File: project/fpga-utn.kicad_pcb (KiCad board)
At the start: 2 copper layers, 76 parts, among them J1 USB_C_Receptacle_USB2.0_16P, U1 LD1117S33TR_SOT223, U2 LD1117S12TR_SOT223, U3 USBLC6-2SC6, U4 FT2232HL, U5 M93C66, U6 ICE40HX4K-TQ144, U7 W25X40CLSN, X1 ECS-3225MV-120-BN-TR

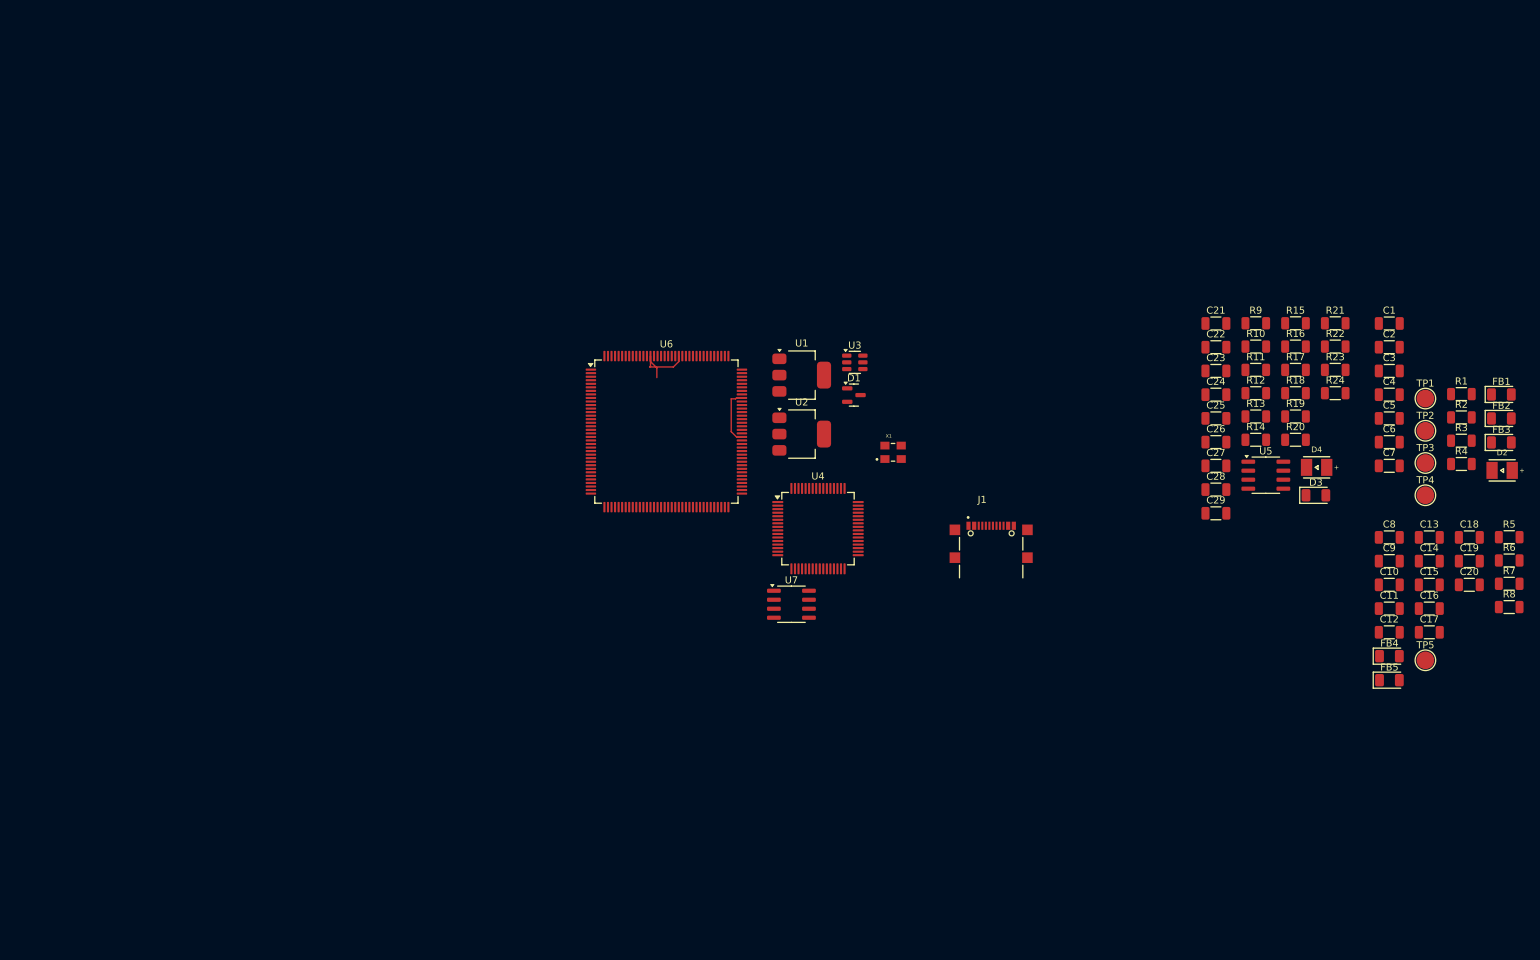
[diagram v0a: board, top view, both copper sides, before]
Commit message: Eliminación de archivos de respaldo y correcciones en la biblioteca de componentes. Se eliminaron archivos de autosave, archivos de esquemas y modelos 3D no utilizados, así como modificaciones en las propiedades de algunos componentes en la biblioteca.
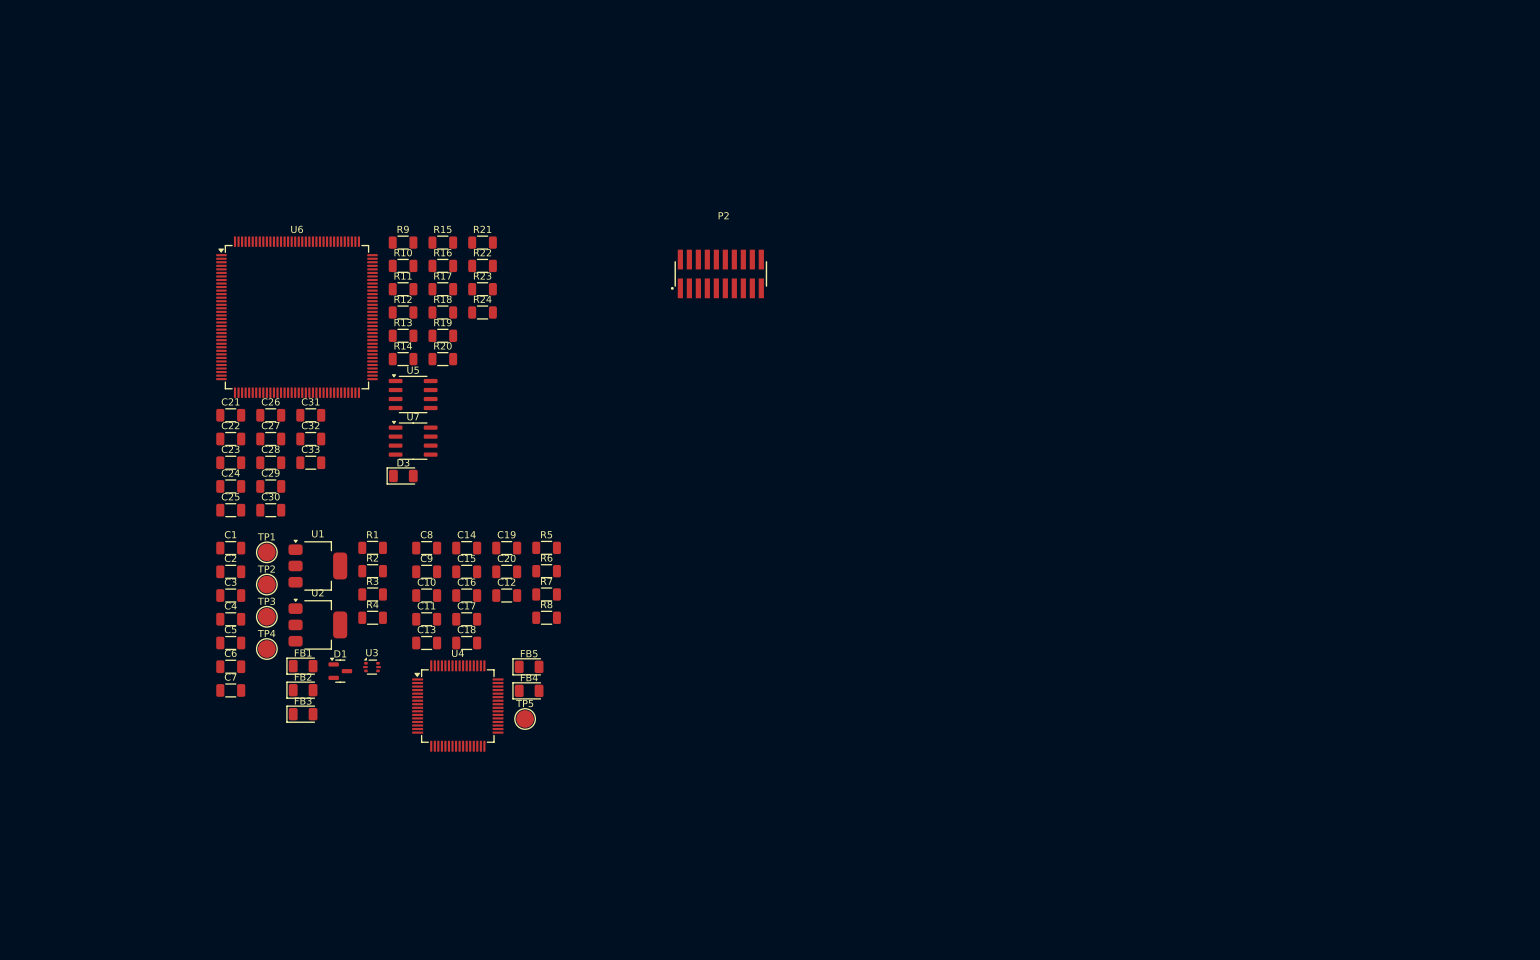
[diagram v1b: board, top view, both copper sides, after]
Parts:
- removed D2, D4: LED, libraries:WL-SMTW_3528
- removed J1: USB_C_Receptacle_USB2.0_16P, libraries:AMPHENOL_GSB1C41110SSHR
- removed X1: ECS-3225MV-120-BN-TR, libraries:OSC_ECS-3225MV-120-BN-TR
- added C30: 100n, Capacitor_SMD:C_1206_3216Metric, F.Cu at (83.5, 87.7)
- added C31: 100n, Capacitor_SMD:C_1206_3216Metric, F.Cu at (89.1, 74.3)
- added C32: 100n, Capacitor_SMD:C_1206_3216Metric, F.Cu at (89.1, 77.7)
- added C33: 100n, Capacitor_SMD:C_1206_3216Metric, F.Cu at (89.1, 81.0)
- added P2: Conector SMD 2x10, FRT-FPGA:Header 2x10 SMD, F.Cu at (147.2, 54.1)
- C21: value 100n -> 10u
- C22: value 10n -> 100n
- C23, C25: value 1u -> 100n
- C24: value 10n -> 10u
- C26, C28: value 10u -> 10n
- C27, C29: value 100n -> 1u
- R10: value 10k -> 2k2
- R11: value 10k -> 100
- R12, R20: value 220 -> 10k
- R13: value R -> 10k
- R14: value R -> 220
- R17, R18: value 10k -> R
- R19: value 220R -> 10k
- R21: value 220 -> 220R
- R22: value 1k -> 220
- R23: value 100 -> 220
- R24: value 100 -> 1k
- R9: value 2k2 -> 100
- U3: footprint Package_TO_SOT_SMD:SOT-23-6 -> Package_TO_SOT_SMD:SOT-666
- moved FB1 173.5 mm to (88.1, 109.7)
- moved FB2 173.5 mm to (88.1, 113.1)
- moved FB3 173.5 mm to (88.1, 116.5)
- moved C1 166.6 mm to (77.8, 93.1)
- moved C2 166.6 mm to (77.8, 96.4)
- moved C3 166.6 mm to (77.8, 99.8)
- moved C4 166.6 mm to (77.8, 103.1)
- moved C5 166.6 mm to (77.8, 106.5)
- moved C6 166.6 mm to (77.8, 109.8)
- moved C7 166.6 mm to (77.8, 113.2)
- moved TP1 165.0 mm to (82.9, 93.7)
- moved TP2 165.0 mm to (82.9, 98.2)
- moved TP3 165.0 mm to (82.9, 102.8)
- moved TP4 165.0 mm to (82.9, 107.3)
- moved R1 155.2 mm to (97.9, 93.0)
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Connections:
- net /FPGA/VUART_CTS renamed /Perifericos/VUART_CTS
- net /FPGA/VUART_DCD renamed /Perifericos/VUART_DCD
- net /FPGA/VUART_DSR renamed /Perifericos/VUART_DSR
- net /FPGA/VUART_DTR renamed /Perifericos/VUART_DTR
- net /FPGA/VUART_RTS renamed /Perifericos/VUART_RTS
- net /FPGA/VUART_Rx renamed /Perifericos/VUART_Rx
- net /FPGA/VUART_Tx renamed /Perifericos/VUART_Tx
- net /Memorias/EEPROM_CLK renamed /Memorias y PLL/EEPROM_CLK
- net /Memorias/EEPROM_CS renamed /Memorias y PLL/EEPROM_CS
- net /Memorias/Flash_SCK renamed /Memorias y PLL/Flash_SCK
- C21 pad 1: +3V3 -> /Memorias y PLL/GNDPLL1
- C21 pad 2: GND -> /Memorias y PLL/VCCPLL1
- C22 pad 1: +3V3 -> /Memorias y PLL/GNDPLL1
- C22 pad 2: GND -> /Memorias y PLL/VCCPLL1
- C24 pad 1: +3V3 -> /Memorias y PLL/VCCPLL2
- C24 pad 2: GND -> /Memorias y PLL/GNDPLL2
- C25 pad 1: +3V3 -> /Memorias y PLL/VCCPLL2
- C25 pad 2: GND -> /Memorias y PLL/GNDPLL2
- C26 pad 1: /Memorias/GNDPLL1 -> +3V3
- C26 pad 2: /Memorias/VCCPLL1 -> GND
- C27 pad 1: /Memorias/GNDPLL1 -> +3V3
- C27 pad 2: /Memorias/VCCPLL1 -> GND
- C28 pad 1: /Memorias/VCCPLL2 -> +3V3
- C28 pad 2: /Memorias/GNDPLL2 -> GND
- C29 pad 1: /Memorias/VCCPLL2 -> +3V3
- C29 pad 2: /Memorias/GNDPLL2 -> GND
- R10 pad 1: +3V3 -> /Memorias y PLL/EEPROM_DATA
- R11 pad 1: +3V3 -> +1V2
- R11 pad 2: Net-(U6E-~{CRESET}) -> /Memorias y PLL/VCCPLL2
- R12 pad 1: Net-(U6E-~{CRESET}) -> +3V3
- R12 pad 2: /Memorias/Flash_RESET -> Net-(U5-DO)
- R13 pad 1: /Memorias/Flash_DI -> +3V3
- R13 pad 2: Net-(U6E-IOB_105_SDO) -> Net-(U6E-~{CRESET})
- R14 pad 1: /Memorias/Flash_DO -> Net-(U6E-~{CRESET})
- R14 pad 2: Net-(U6E-IOB_106_SDI) -> /Memorias y PLL/Flash_RESET
- R15 pad 1: unconnected-(R15-Pad1) -> /Memorias y PLL/Flash_DI
- R15 pad 2: Net-(U6E-IOB_107_SCK) -> Net-(U6E-IOB_105_SDO)
- R16 pad 1: /Memorias/Flash_CS -> /Memorias y PLL/Flash_DO
- R16 pad 2: Net-(U6E-IOB_108_SS) -> Net-(U6E-IOB_106_SDI)
- R17 pad 1: +3V3 -> unconnected-(R17-Pad1)
- R17 pad 2: Net-(U6E-IOB_108_SS) -> Net-(U6E-IOB_107_SCK)
- R18 pad 1: +3V3 -> /Memorias y PLL/Flash_CS
- R18 pad 2: Net-(U6E-IOB_107_SCK) -> Net-(U6E-IOB_108_SS)
- R19 pad 1: /Memorias/Flash_DONE -> +3V3
- R19 pad 2: Net-(D4-A) -> Net-(U6E-IOB_108_SS)
- R20 pad 1: Net-(U7-~{WP}) -> +3V3
- R20 pad 2: +3V3 -> Net-(U6E-IOB_107_SCK)
- R21 pad 1: +3V3 -> /Memorias y PLL/Flash_DONE
- R21 pad 2: Net-(U7-~{HOLD}) -> Net-(D4-A)
- R22 pad 1: Net-(D4-A) -> Net-(U7-~{WP})
- R23 pad 1: +1V2 -> +3V3
- R23 pad 2: /Memorias/VCCPLL1 -> Net-(U7-~{HOLD})
- R24 pad 1: +1V2 -> Net-(D4-A)
- R24 pad 2: /Memorias/VCCPLL2 -> +3V3
- R9 pad 1: /Memorias/EEPROM_DATA -> +1V2
- R9 pad 2: Net-(U5-DO) -> /Memorias y PLL/VCCPLL1
- U4 pad 17: /Memorias/Flash_DI -> /Memorias y PLL/Flash_DI
- U4 pad 18: /Memorias/Flash_DO -> /Memorias y PLL/Flash_DO
- U4 pad 21: /Memorias/Flash_CS -> /Memorias y PLL/Flash_CS
- U4 pad 23: /Memorias/Flash_DONE -> /Memorias y PLL/Flash_DONE
- U4 pad 24: /Memorias/Flash_RESET -> /Memorias y PLL/Flash_RESET
- U4 pad 61: /Memorias/EEPROM_DATA -> /Memorias y PLL/EEPROM_DATA
- U5 pad 3: /Memorias/EEPROM_DATA -> /Memorias y PLL/EEPROM_DATA
- U6 pad 111: Net-(U6E-VCC-Pad111) -> +1V2
- U6 pad 126: /Memorias/VCCPLL1 -> /Memorias y PLL/VCCPLL1
- U6 pad 127: /Memorias/GNDPLL1 -> /Memorias y PLL/GNDPLL1
- U6 pad 27: Net-(U6E-VCC-Pad111) -> +1V2
- U6 pad 40: Net-(U6E-VCC-Pad111) -> +1V2
- U6 pad 53: /Memorias/GNDPLL2 -> /Memorias y PLL/GNDPLL2
- U6 pad 54: /Memorias/VCCPLL2 -> /Memorias y PLL/VCCPLL2
- U6 pad 92: Net-(U6E-VCC-Pad111) -> +1V2
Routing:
- net Net-(U6A-VCCIO_0-Pad123): track 10.2 -> 0.00 mm
- net Net-(U6B-VCCIO_1-Pad100): track 8.02 -> 0.00 mm

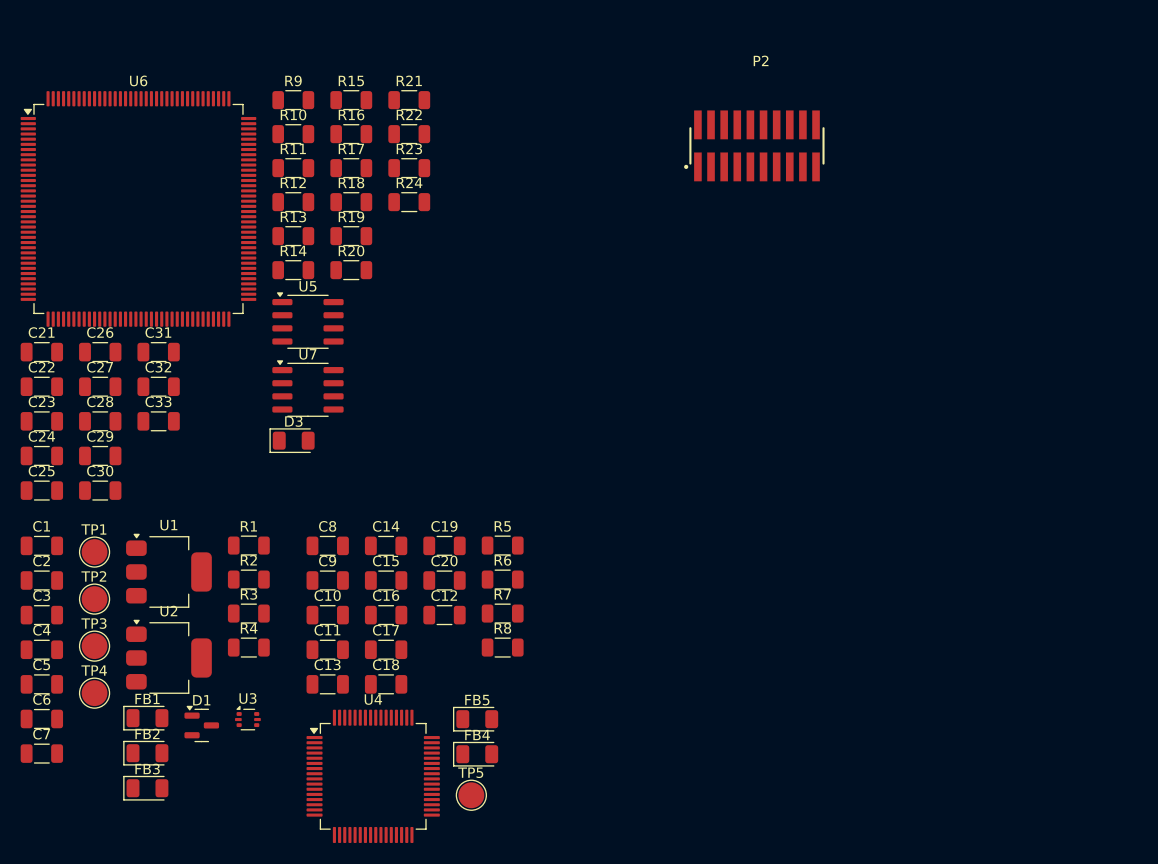
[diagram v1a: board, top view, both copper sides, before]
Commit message: - Included properties such as Reference, Value, Footprint, and various manufacturer details. - Defined 20 pins with appropriate names and attributes for the symbol. - Ensured compatibility with KiCad version 8.0 and above.
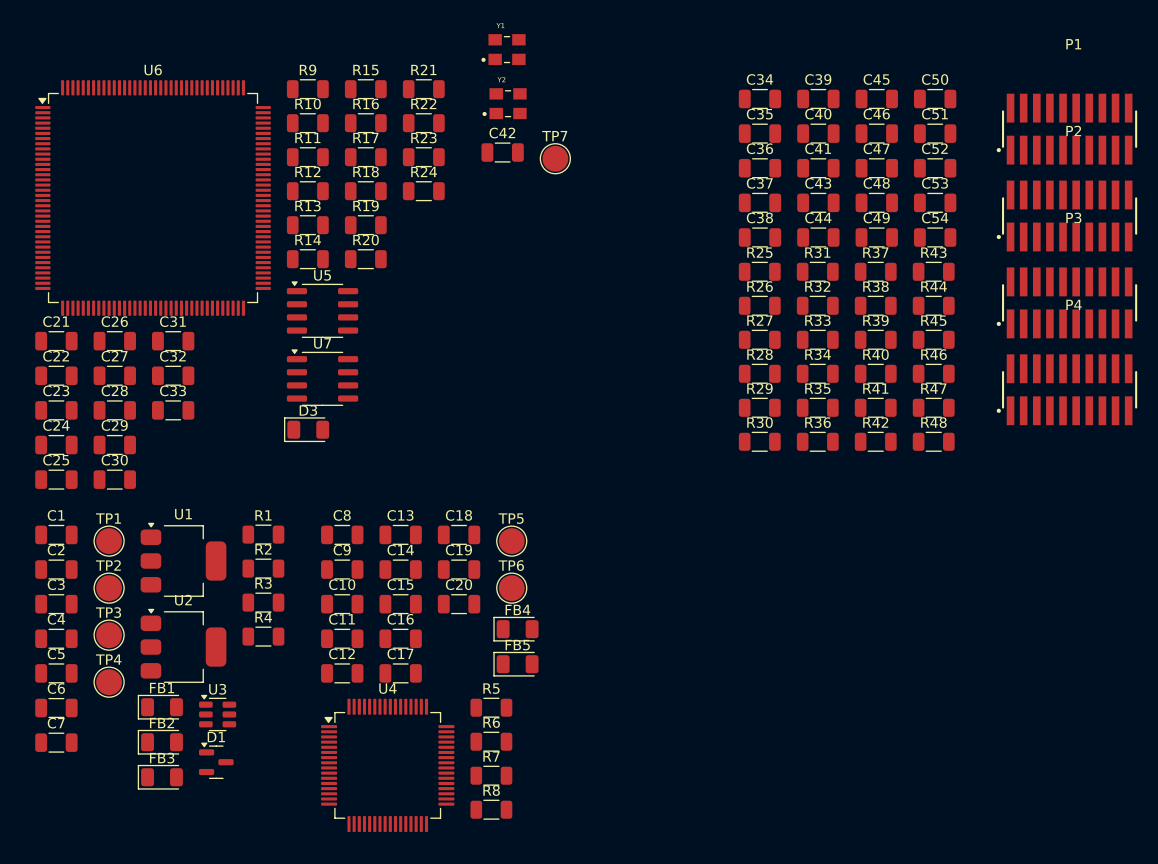
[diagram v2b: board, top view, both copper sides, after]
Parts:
- added C34: 10uF, Capacitor_SMD:C_1206_3216Metric, F.Cu at (147.3, 49.8)
- added C35: 10uF, Capacitor_SMD:C_1206_3216Metric, F.Cu at (147.3, 53.2)
- added C36: 10uF, Capacitor_SMD:C_1206_3216Metric, F.Cu at (147.3, 56.5)
- added C37: 10uF, Capacitor_SMD:C_1206_3216Metric, F.Cu at (147.3, 59.9)
- added C38: 10uF, Capacitor_SMD:C_1206_3216Metric, F.Cu at (147.3, 63.2)
- added C39: 10uF, Capacitor_SMD:C_1206_3216Metric, F.Cu at (153.0, 49.8)
- added C40: 10uF, Capacitor_SMD:C_1206_3216Metric, F.Cu at (153.0, 53.2)
- added C41: 10uF, Capacitor_SMD:C_1206_3216Metric, F.Cu at (153.0, 56.5)
- added C42: 100n, Capacitor_SMD:C_1206_3216Metric, F.Cu at (122.4, 55.0)
- added C43: 1uF, Capacitor_SMD:C_1206_3216Metric, F.Cu at (153.0, 59.9)
- added C44: 100n, Capacitor_SMD:C_1206_3216Metric, F.Cu at (153.0, 63.2)
- added C45: 100n, Capacitor_SMD:C_1206_3216Metric, F.Cu at (158.6, 49.8)
- added C46: 1uF, Capacitor_SMD:C_1206_3216Metric, F.Cu at (158.6, 53.2)
- added C47: 100n, Capacitor_SMD:C_1206_3216Metric, F.Cu at (158.6, 56.5)
- added C48: 100n, Capacitor_SMD:C_1206_3216Metric, F.Cu at (158.6, 59.9)
- added C49: 1uF, Capacitor_SMD:C_1206_3216Metric, F.Cu at (158.6, 63.2)
- added C50: 100n, Capacitor_SMD:C_1206_3216Metric, F.Cu at (164.3, 49.8)
- added C51: 100n, Capacitor_SMD:C_1206_3216Metric, F.Cu at (164.3, 53.2)
- added C52: 1uF, Capacitor_SMD:C_1206_3216Metric, F.Cu at (164.3, 56.5)
- added C53: 100n, Capacitor_SMD:C_1206_3216Metric, F.Cu at (164.3, 59.9)
- added C54: 100n, Capacitor_SMD:C_1206_3216Metric, F.Cu at (164.3, 63.2)
- added P1: Conector SMD 2x10, FRT-FPGA:Header 2x10 SMD, F.Cu at (177.4, 52.5)
- added P3: Conector SMD 2x10, FRT-FPGA:Header 2x10 SMD, F.Cu at (177.4, 69.3)
- added P4: Conector SMD 2x10, FRT-FPGA:Header 2x10 SMD, F.Cu at (177.4, 77.7)
- added R25: R, Resistor_SMD:R_1206_3216Metric, F.Cu at (147.3, 66.5)
- added R26: R, Resistor_SMD:R_1206_3216Metric, F.Cu at (147.3, 69.8)
- added R27: R, Resistor_SMD:R_1206_3216Metric, F.Cu at (147.3, 73.1)
- added R28: R, Resistor_SMD:R_1206_3216Metric, F.Cu at (147.3, 76.4)
- added R29: R, Resistor_SMD:R_1206_3216Metric, F.Cu at (147.3, 79.7)
- added R30: R, Resistor_SMD:R_1206_3216Metric, F.Cu at (147.3, 83.0)
- added R31: R, Resistor_SMD:R_1206_3216Metric, F.Cu at (152.9, 66.5)
- added R32: R, Resistor_SMD:R_1206_3216Metric, F.Cu at (152.9, 69.8)
- added R33: 220, Resistor_SMD:R_1206_3216Metric, F.Cu at (152.9, 73.1)
- added R34: 220, Resistor_SMD:R_1206_3216Metric, F.Cu at (152.9, 76.4)
- added R35: 220, Resistor_SMD:R_1206_3216Metric, F.Cu at (152.9, 79.7)
- added R36: 220, Resistor_SMD:R_1206_3216Metric, F.Cu at (152.9, 83.0)
- added R37: 220, Resistor_SMD:R_1206_3216Metric, F.Cu at (158.5, 66.5)
- added R38: 220, Resistor_SMD:R_1206_3216Metric, F.Cu at (158.5, 69.8)
- added R39: 220, Resistor_SMD:R_1206_3216Metric, F.Cu at (158.5, 73.1)
- added R40: 220, Resistor_SMD:R_1206_3216Metric, F.Cu at (158.5, 76.4)
- added R41: 10k, Resistor_SMD:R_1206_3216Metric, F.Cu at (158.5, 79.7)
- added R42: 10k, Resistor_SMD:R_1206_3216Metric, F.Cu at (158.5, 83.0)
- added R43: 10k, Resistor_SMD:R_1206_3216Metric, F.Cu at (164.1, 66.5)
- added R44: 10k, Resistor_SMD:R_1206_3216Metric, F.Cu at (164.1, 69.8)
- added R45: 10k, Resistor_SMD:R_1206_3216Metric, F.Cu at (164.1, 73.1)
- added R46: 10k, Resistor_SMD:R_1206_3216Metric, F.Cu at (164.1, 76.4)
- added R47: 10k, Resistor_SMD:R_1206_3216Metric, F.Cu at (164.1, 79.7)
- added R48: 10k, Resistor_SMD:R_1206_3216Metric, F.Cu at (164.1, 83.0)
- added TP6: 12MHZ, TestPoint:TestPoint_Pad_D2.5mm, F.Cu at (123.3, 97.2)
- added TP7: 100MHZ, TestPoint:TestPoint_Pad_D2.5mm, F.Cu at (127.5, 55.6)
- added Y1: ECS-3225MV-120-CN-TR, ECS_3225MV_120_CN_TR:OSC_ECS-3225MV-120-CN-TR, F.Cu at (122.8, 45.0)
- added Y2: ECS-3225MVQ-1000-CN-TR, ECS_3225MV_120_CN_TR:OSC_ECS-3225MV-120-CN-TR, F.Cu at (123.0, 50.3)
- TP1: value TP2_3V1 -> TP1_5V1
- TP2: value TP1_5V1 -> TP2_3V1
- U3: footprint Package_TO_SOT_SMD:SOT-666 -> Package_TO_SOT_SMD:SOT-23-6
- moved P2 31.0 mm to (177.4, 60.9)
- moved TP5 24.9 mm to (123.3, 92.6)
- moved C13 16.1 mm to (112.6, 92.0)
- moved C18 16.1 mm to (118.2, 92.0)
- moved R5 15.7 mm to (121.3, 108.7)
- moved R6 15.7 mm to (121.3, 112.0)
- moved R7 15.7 mm to (121.3, 115.3)
- moved R8 15.7 mm to (121.3, 118.6)
- moved FB4 12.7 mm to (123.9, 101.1)
- moved C12 11.4 mm to (106.9, 105.4)
- moved FB5 6.60 mm to (123.9, 104.5)
- moved D1 3.83 mm to (94.7, 114.0)
- moved U3 2.97 mm to (94.8, 109.4)
- moved C14 2.69 mm to (112.6, 95.4)
- moved C16 2.69 mm to (112.6, 102.1)
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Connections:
- C17 pad 2: Net-(X1-GND) -> GND
- P2 pad 3V3: Net-(P2-3V3-Pad3V3_2) -> +3V3
- P2 pad 3V3_2: Net-(P2-3V3-Pad3V3_2) -> +3V3
- P2 pad 5V: Net-(P2-5V-Pad5V_2) -> +5V
- P2 pad 5V_2: Net-(P2-5V-Pad5V_2) -> +5V
- P2 pad GND: Net-(P2-GND-PadGND_2) -> GND
- P2 pad GND_2: Net-(P2-GND-PadGND_2) -> GND
- P2 pad IO1: unconnected-(P2-PadIO1) -> Net-(U6D-IOL_13A)
- P2 pad IO10: unconnected-(P2-PadIO10) -> Net-(U6D-IOL_23B)
- P2 pad IO11: unconnected-(P2-PadIO11) -> Net-(U6D-IOL_24A)
- P2 pad IO12: unconnected-(P2-PadIO12) -> Net-(U6D-IOL_24B)
- P2 pad IO13: unconnected-(P2-PadIO13) -> Net-(U6D-IOL_25A)
- P2 pad IO14: unconnected-(P2-PadIO14) -> Net-(U6D-IOL_25B)
- P2 pad IO2: unconnected-(P2-PadIO2) -> Net-(U6D-IOL_13B_GBIN7)
- P2 pad IO3: unconnected-(P2-PadIO3) -> Net-(U6D-IOL_14A_GBIN6)
- P2 pad IO4: unconnected-(P2-PadIO4) -> Net-(U6D-IOL_14B)
- P2 pad IO5: unconnected-(P2-PadIO5) -> Net-(U6D-IOL_17A)
- P2 pad IO6: Net-(P2-3V3-Pad3V3_2) -> Net-(U6D-IOL_17B)
- P2 pad IO7: unconnected-(P2-PadIO7) -> Net-(U6D-IOL_18A)
- P2 pad IO8: unconnected-(P2-PadIO8) -> Net-(U6D-IOL_18B)
- P2 pad IO9: unconnected-(P2-PadIO9) -> Net-(U6D-IOL_23A)
- R17 pad 1: unconnected-(R17-Pad1) -> /Memorias y PLL/Flash_SCK
- TP1 pad 1: +3V3 -> +5V
- TP2 pad 1: +5V -> +3V3
- U6 pad 1: unconnected-(U6D-IOL_2A-Pad1) -> Net-(U6D-IOL_2A)
- U6 pad 10: unconnected-(U6D-IOL_5B-Pad10) -> Net-(U6D-IOL_5B)
- U6 pad 100: Net-(U6B-VCCIO_1-Pad100) -> +3V3
- U6 pad 101: unconnected-(U6B-IOR_160-Pad101) -> Net-(U6B-IOR_160)
- U6 pad 102: unconnected-(U6B-IOR_161-Pad102) -> Net-(U6B-IOR_161)
- U6 pad 104: unconnected-(U6B-IOR_164-Pad104) -> Net-(U6B-IOR_164)
- U6 pad 105: unconnected-(U6B-IOR_165-Pad105) -> Net-(U6B-IOR_165)
- U6 pad 106: unconnected-(U6B-IOR_166-Pad106) -> Net-(U6B-IOR_166)
- U6 pad 107: unconnected-(U6B-IOR_167-Pad107) -> Net-(U6B-IOR_167)
- U6 pad 11: unconnected-(U6D-IOL_8A-Pad11) -> Net-(U6D-IOL_8A)
- U6 pad 110: unconnected-(U6A-IOT_168-Pad110) -> /Perifericos/LED1
- U6 pad 112: unconnected-(U6A-IOT_169-Pad112) -> /Perifericos/LED2
- U6 pad 113: unconnected-(U6A-IOT_170-Pad113) -> /Perifericos/LED3
- U6 pad 114: unconnected-(U6A-IOT_171-Pad114) -> /Perifericos/LED4
- U6 pad 115: unconnected-(U6A-IOT_172-Pad115) -> /Perifericos/LED5
- U6 pad 116: unconnected-(U6A-IOT_173-Pad116) -> /Perifericos/LED6
- U6 pad 117: unconnected-(U6A-IOT_174-Pad117) -> /Perifericos/LED7
- U6 pad 118: unconnected-(U6A-IOT_177-Pad118) -> /Perifericos/LED8
- U6 pad 12: unconnected-(U6D-IOL_8B-Pad12) -> Net-(U6D-IOL_8B)
- U6 pad 123: Net-(U6A-VCCIO_0-Pad123) -> +3V3
- U6 pad 131: Net-(U6A-VCCIO_0-Pad123) -> +3V3
- U6 pad 136: unconnected-(U6A-IOT_214-Pad136) -> /Perifericos/BOT8
- U6 pad 137: unconnected-(U6A-IOT_215-Pad137) -> /Perifericos/BOT7
- U6 pad 138: unconnected-(U6A-IOT_216-Pad138) -> /Perifericos/BOT6
- U6 pad 139: unconnected-(U6A-IOT_217-Pad139) -> /Perifericos/BOT5
- U6 pad 141: unconnected-(U6A-IOT_219-Pad141) -> /Perifericos/BOT4
- U6 pad 142: unconnected-(U6A-IOT_220-Pad142) -> /Perifericos/BOT3
- U6 pad 143: unconnected-(U6A-IOT_221-Pad143) -> /Perifericos/BOT2
- U6 pad 144: unconnected-(U6A-IOT_222-Pad144) -> /Perifericos/BOT1
- U6 pad 15: unconnected-(U6D-IOL_10A-Pad15) -> Net-(U6D-IOL_10A)
- U6 pad 16: unconnected-(U6D-IOL_10B-Pad16) -> Net-(U6D-IOL_10B)
- U6 pad 17: unconnected-(U6D-IOL_12A-Pad17) -> Net-(U6D-IOL_12A)
- U6 pad 18: unconnected-(U6D-IOL_12B-Pad18) -> Net-(U6D-IOL_12B)
- U6 pad 19: unconnected-(U6D-IOL_13A-Pad19) -> Net-(U6D-IOL_13A)
- U6 pad 2: unconnected-(U6D-IOL_2B-Pad2) -> Net-(U6D-IOL_2B)
- U6 pad 20: unconnected-(U6D-IOL_13B_GBIN7-Pad20) -> Net-(U6D-IOL_13B_GBIN7)
- U6 pad 21: unconnected-(U6D-IOL_14A_GBIN6-Pad21) -> Net-(U6D-IOL_14A_GBIN6)
- U6 pad 22: unconnected-(U6D-IOL_14B-Pad22) -> Net-(U6D-IOL_14B)
- U6 pad 23: unconnected-(U6D-IOL_17A-Pad23) -> Net-(U6D-IOL_17A)
- U6 pad 24: unconnected-(U6D-IOL_17B-Pad24) -> Net-(U6D-IOL_17B)
- U6 pad 25: unconnected-(U6D-IOL_18A-Pad25) -> Net-(U6D-IOL_18A)
- U6 pad 26: unconnected-(U6D-IOL_18B-Pad26) -> Net-(U6D-IOL_18B)
- U6 pad 28: unconnected-(U6D-IOL_23A-Pad28) -> Net-(U6D-IOL_23A)
- U6 pad 29: unconnected-(U6D-IOL_23B-Pad29) -> Net-(U6D-IOL_23B)
- U6 pad 3: unconnected-(U6D-IOL_3A-Pad3) -> Net-(U6D-IOL_3A)
- U6 pad 30: Net-(U6D-VCCIO_3-Pad30) -> +3V3
- U6 pad 31: unconnected-(U6D-IOL_24A-Pad31) -> Net-(U6D-IOL_24A)
- U6 pad 32: unconnected-(U6D-IOL_24B-Pad32) -> Net-(U6D-IOL_24B)
- U6 pad 33: unconnected-(U6D-IOL_25A-Pad33) -> Net-(U6D-IOL_25A)
- U6 pad 34: unconnected-(U6D-IOL_25B-Pad34) -> Net-(U6D-IOL_25B)
- U6 pad 4: unconnected-(U6D-IOL_3B-Pad4) -> Net-(U6D-IOL_3B)
- U6 pad 46: Net-(U6C-VCCIO_2-Pad46) -> +3V3
- U6 pad 49: unconnected-(U6C-IOB_81_GBIN5-Pad49) -> Net-(U6C-IOB_81_GBIN5)
- U6 pad 57: Net-(U6C-VCCIO_2-Pad46) -> +3V3
- U6 pad 6: Net-(U6D-VCCIO_3-Pad30) -> +3V3
- U6 pad 7: unconnected-(U6D-IOL_4A-Pad7) -> Net-(U6D-IOL_4A)
- U6 pad 73: unconnected-(U6B-IOR_109-Pad73) -> Net-(U6B-IOR_109)
- U6 pad 74: unconnected-(U6B-IOR_110-Pad74) -> Net-(U6B-IOR_110)
- U6 pad 75: unconnected-(U6B-IOR_111-Pad75) -> Net-(U6B-IOR_111)
- U6 pad 76: unconnected-(U6B-IOR_112-Pad76) -> Net-(U6B-IOR_112)
- U6 pad 78: unconnected-(U6B-IOR_114-Pad78) -> Net-(U6B-IOR_114)
- U6 pad 79: unconnected-(U6B-IOR_115-Pad79) -> Net-(U6B-IOR_115)
- U6 pad 8: unconnected-(U6D-IOL_4B-Pad8) -> Net-(U6D-IOL_4B)
- U6 pad 80: unconnected-(U6B-IOR_116-Pad80) -> Net-(U6B-IOR_116)
- U6 pad 81: unconnected-(U6B-IOR_117-Pad81) -> Net-(U6B-IOR_117)
- U6 pad 82: unconnected-(U6B-IOR_118-Pad82) -> Net-(U6B-IOR_118)
- U6 pad 83: unconnected-(U6B-IOR_119-Pad83) -> Net-(U6B-IOR_119)
- U6 pad 84: unconnected-(U6B-IOR_120-Pad84) -> Net-(U6B-IOR_120)
- U6 pad 85: unconnected-(U6B-IOR_128-Pad85) -> Net-(U6B-IOR_128)
- U6 pad 87: unconnected-(U6B-IOR_136-Pad87) -> Net-(U6B-IOR_136)
- U6 pad 88: unconnected-(U6B-IOR_137-Pad88) -> Net-(U6B-IOR_137)
- U6 pad 89: Net-(U6B-VCCIO_1-Pad100) -> +3V3
- U6 pad 9: unconnected-(U6D-IOL_5A-Pad9) -> Net-(U6D-IOL_5A)
- U6 pad 91: unconnected-(U6B-IOR_139-Pad91) -> Net-(U6B-IOR_139)
- U6 pad 93: unconnected-(U6B-IOR_140_GBIN3-Pad93) -> Net-(U6B-IOR_140_GBIN3)
- U6 pad 94: unconnected-(U6B-IOR_141_GBIN2-Pad94) -> Net-(U6B-IOR_141_GBIN2)
- U6 pad 95: unconnected-(U6B-IOR_144-Pad95) -> Net-(U6B-IOR_144)
- U6 pad 96: unconnected-(U6B-IOR_146-Pad96) -> Net-(U6B-IOR_146)
- U6 pad 97: unconnected-(U6B-IOR_147-Pad97) -> Net-(U6B-IOR_147)
- U6 pad 98: unconnected-(U6B-IOR_148-Pad98) -> Net-(U6B-IOR_148)
- U6 pad 99: unconnected-(U6B-IOR_152-Pad99) -> Net-(U6B-IOR_152)
